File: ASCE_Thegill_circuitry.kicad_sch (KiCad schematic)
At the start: 57 parts, among them J10 Motor Battery, J11 Peripheral Battery, J12 ServoPSU, J2 Arm Servos, J5 RT, J6 RB, J7 BL, J8 TL, J9 Arm Motors, M1 Basket Dump Servo, Q1 NMOS, U1 TB6612FNG, U2 TB6612FNG, U3 RASPBERRY_PI_PICO, U4 Buck_converter, U5 Buck_converter, U6 Buck_converter

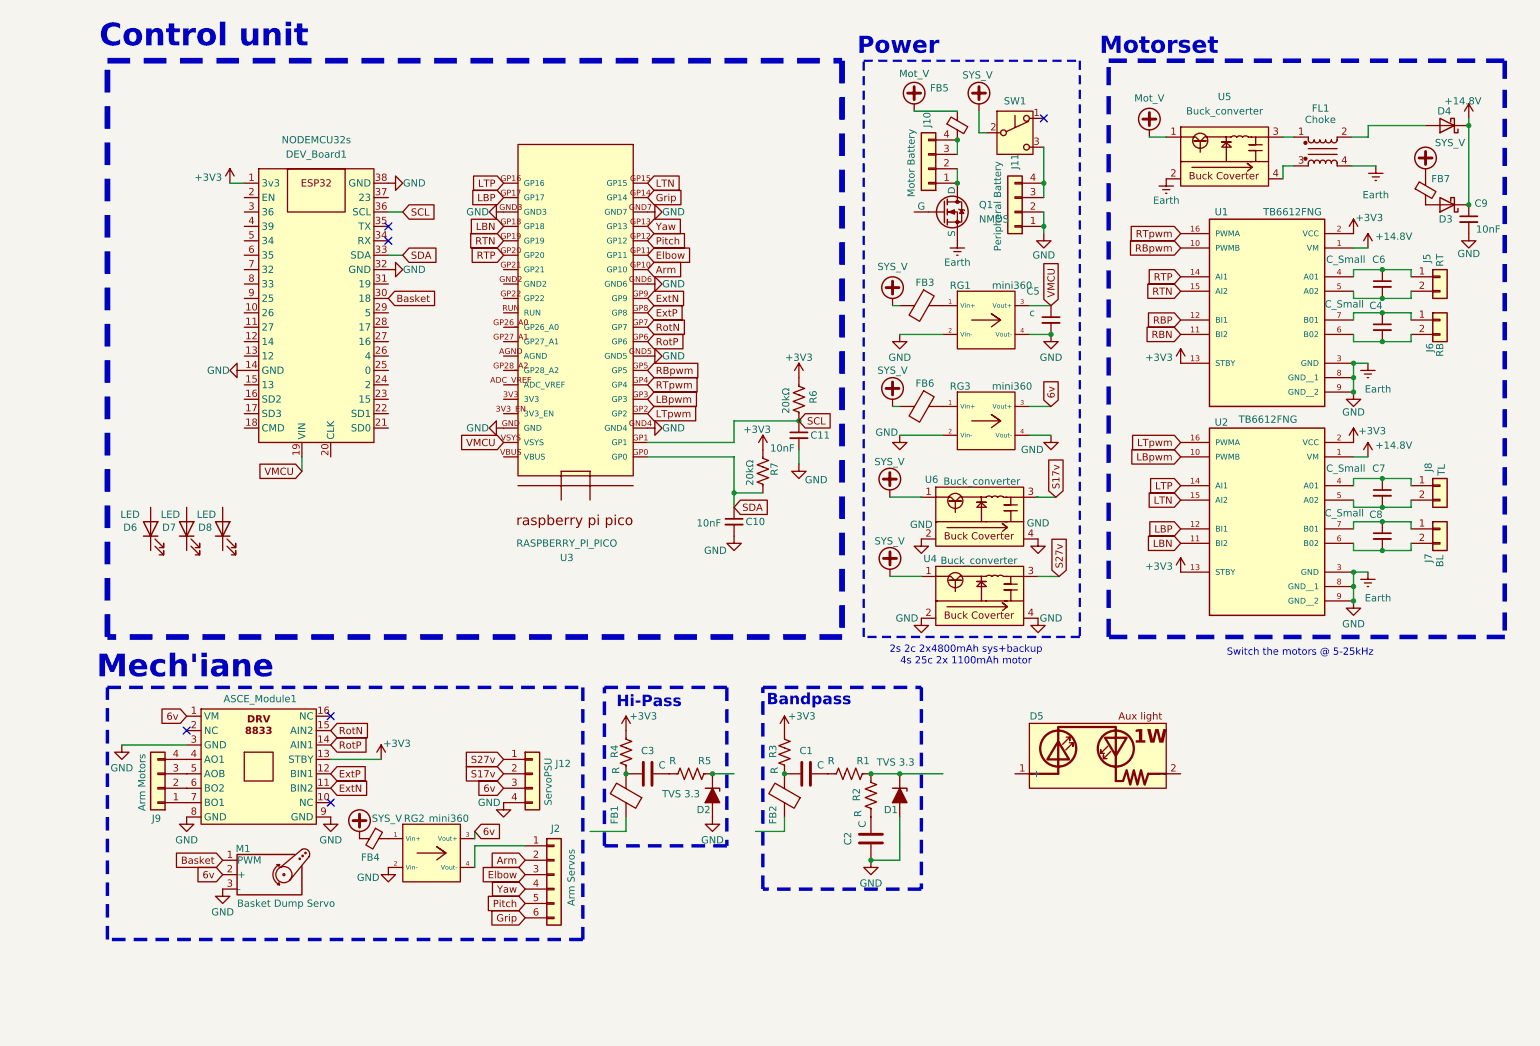
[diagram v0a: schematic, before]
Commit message: Fixed up the LED drivers and probably prepping up some more mechanisms for the motors LIPO
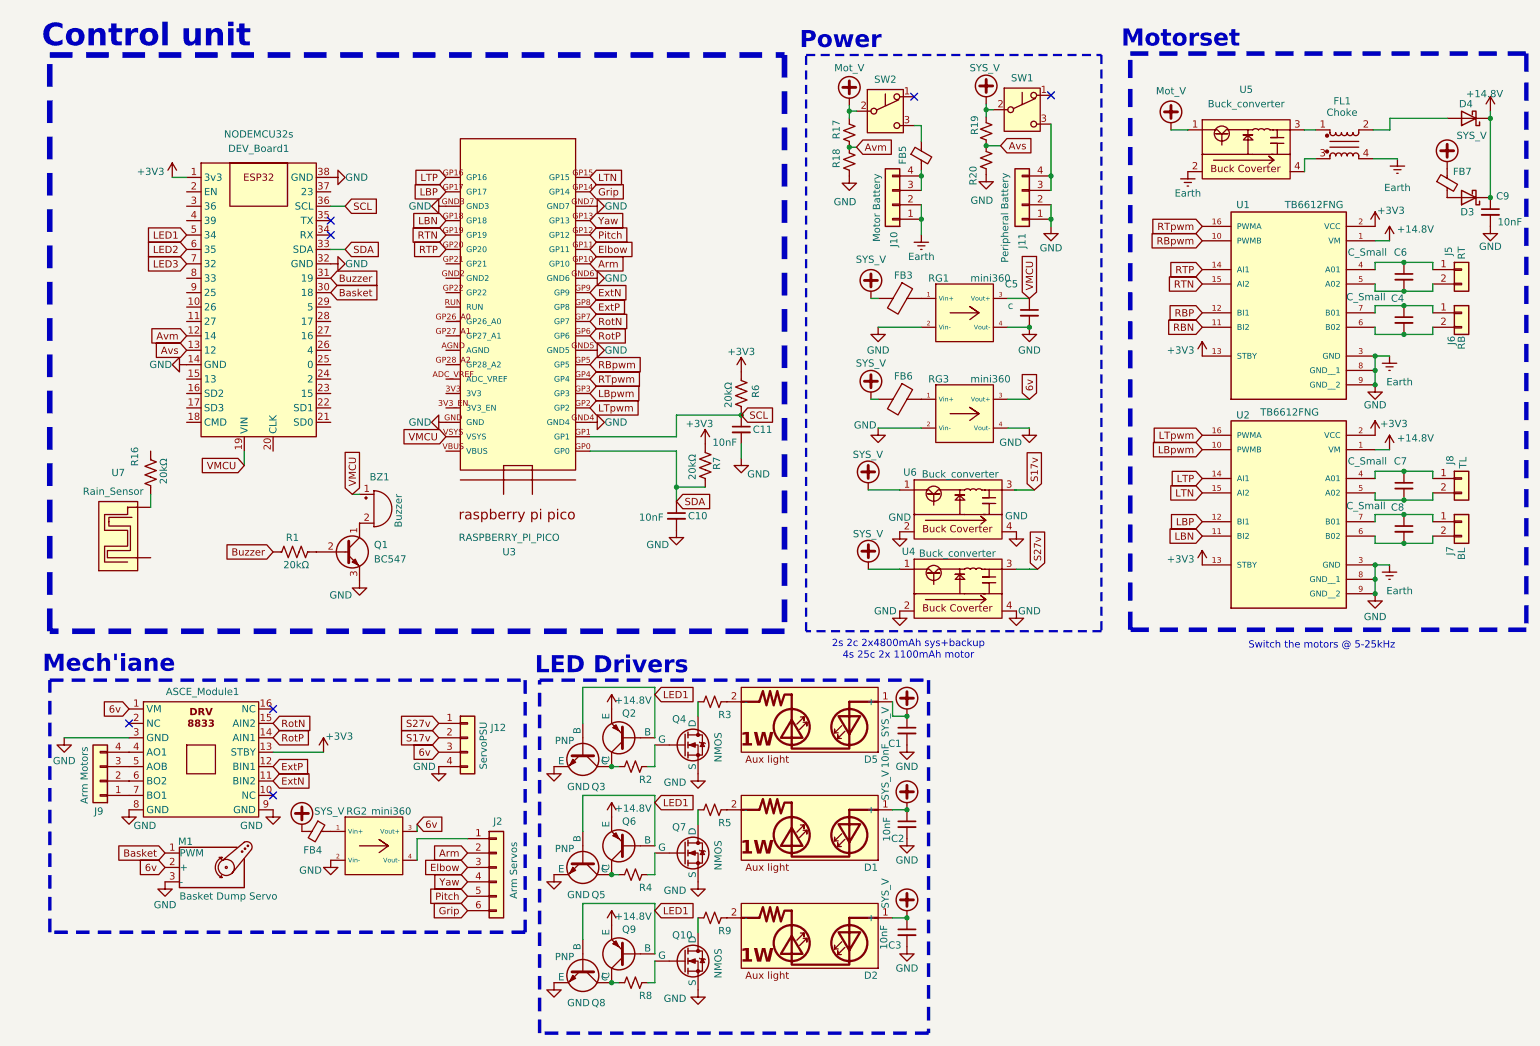
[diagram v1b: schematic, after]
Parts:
- removed C1, C2, C3: C, symbol Device:C
- removed D1, D2: TVS 3.3, symbol Device:D_Zener_Filled
- removed D6, D7, D8: LED, symbol Device:LED
- removed FB1, FB2: FerriteBead, Resistor_THT:R_Axial_DIN0309_L9.0mm_D3.2mm_P12.70mm_Horizontal, symbol Device:FerriteBead
- removed Q1: NMOS, symbol Simulation_SPICE:NMOS
- removed R2, R3, R4, R5: R, symbol Device:R_US
- added BZ1: Buzzer, symbol Device:Buzzer
- added C1, C2, C3: 10nF, symbol Device:C_Small
- added D1, D2: ~, symbol ASCE_Servase:ASCE_LED_Terminal
- added Q1: BC547, Package_TO_SOT_THT:TO-92_Inline, symbol Transistor_BJT:BC547
- added Q10, Q4, Q7: NMOS, symbol Simulation_SPICE:NMOS
- added Q2, Q6, Q9: PNP, symbol Simulation_SPICE:PNP
- added Q3, Q5, Q8: NPN, symbol Simulation_SPICE:NPN
- added R16: 20kΩ, symbol Device:R_US
- added R17, R18, R19, R2, R20, R3, R4, R5, R8, R9: R_Small_US, symbol Device:R_Small_US
- added SW2: ~, symbol Switch:SW_Push_SPDT
- added U7: Rain_Sensor, symbol ASCE_Sensors:Rain_Sensor
- R1: value R -> 20kΩ
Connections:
- net +14.8V: now also Q2.3 (E), Q6.3 (E), Q9.3 (E)
- net Earth: now also J10.1 (Pin_1), J10.2 (Pin_2), C1.2, C2.2, C3.2, Q1.3 (E), Q10.3 (S), Q3.3 (E), Q4.3 (S), Q5.3 (E), Q7.3 (S), Q8.3 (E), R18.1, R20.1
- net Mot_V: now also R17.2, SW2.2 (B); no longer FB5.1
- net SYS_V: now also D5.1 (+), C1.1, C2.1, C3.1, D1.1 (+), D2.1 (+), R19.2
- net VMCU: now also BZ1.1 (+)
- net Buzzer: now reaches R1.1
- net Buzzer: now also DEV_Board1.31 (19)
- net at R1.2: now also Q1.2 (B)
- net Avm: now reaches DEV_Board1.12 (14)
- net Avm: now also R17.1, R18.2
- net Avs: now reaches DEV_Board1.13 (12)
- net Avs: now also R19.1, R20.2
- net LED1: now reaches DEV_Board1.5 (34)
- net LED1: now also Q2.2 (B), Q3.2 (B), Q5.2 (B), Q6.2 (B), Q8.2 (B), Q9.2 (B)
- net LED2: now reaches DEV_Board1.6 (35)
- net LED3: now reaches DEV_Board1.7 (32)
- net at D5.2 (-): now also R3.1
- new net: Q10.1 (D), R9.2
- new net: Q10.2 (G), R8.1
- new net: Q4.2 (G), R2.1
- new net: Q2.1 (C), Q3.1 (C), R2.2
- new net: D2.2 (-), R9.1
- new net: Q4.1 (D), R3.2
- new net: Q8.1 (C), Q9.1 (C), R8.2
- new net: R16.1, U7.
- new net: Q7.2 (G), R4.1
- new net: Q5.1 (C), Q6.1 (C), R4.2
- new net: BZ1.2 (-), Q1.1 (C)
- new net: FB5.1, SW2.3 (C)
- new net: Q7.1 (D), R5.2
- new net: D1.2 (-), R5.1
- no-connect marks 6 -> 7
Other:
- note added: "LED Drivers"
- note removed: "Bandpass"
- note removed: "Hi-Pass"
- moved on the sheet: ASCE_Module1, C10, C11, C4, C5, C6, C7, C8, C9, D3, D4, DEV_Board1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
